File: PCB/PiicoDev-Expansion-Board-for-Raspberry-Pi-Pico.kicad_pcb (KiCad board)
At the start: 2 copper layers, 50.4 x 51.4 mm, 34 parts, among them J1 PiicoDev, J2 JST PH, J3 , J4 , Q1 MOSFET P-CH

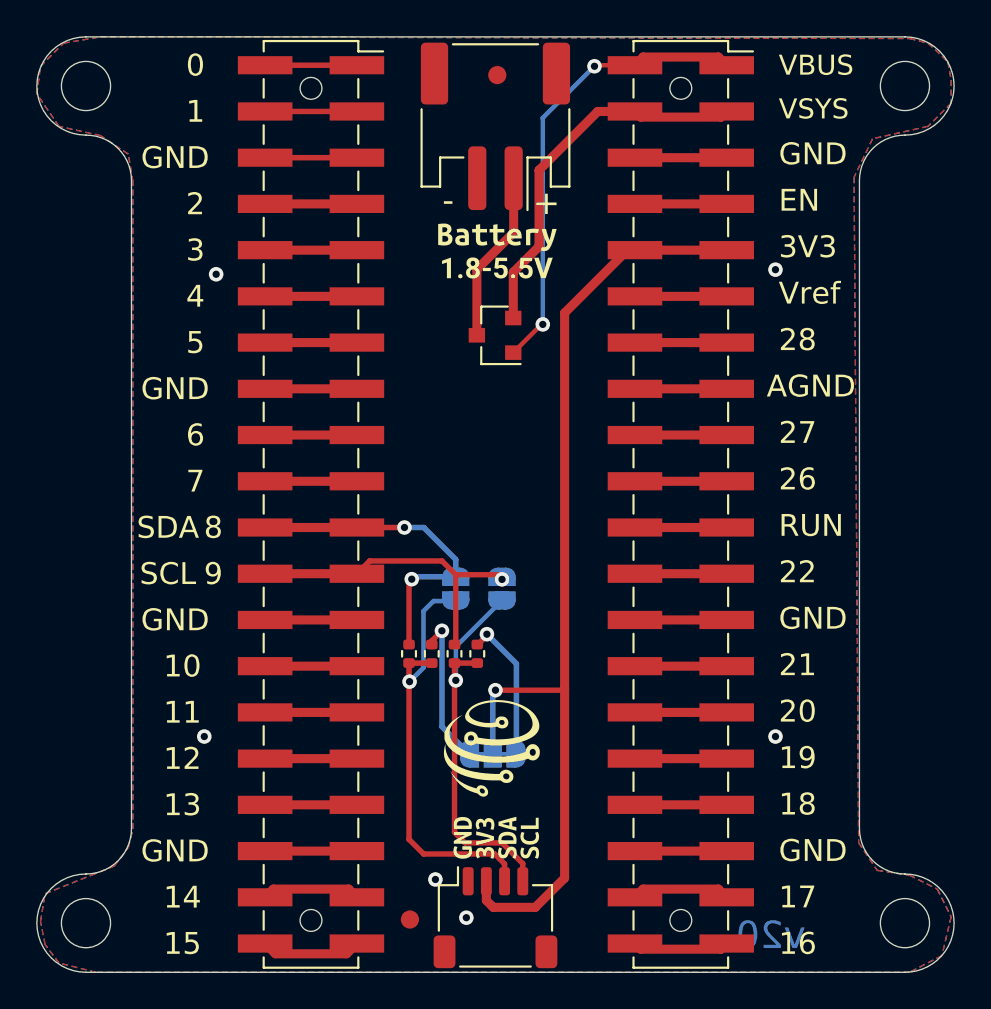
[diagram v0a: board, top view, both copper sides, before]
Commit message: Wide voltage expansion board
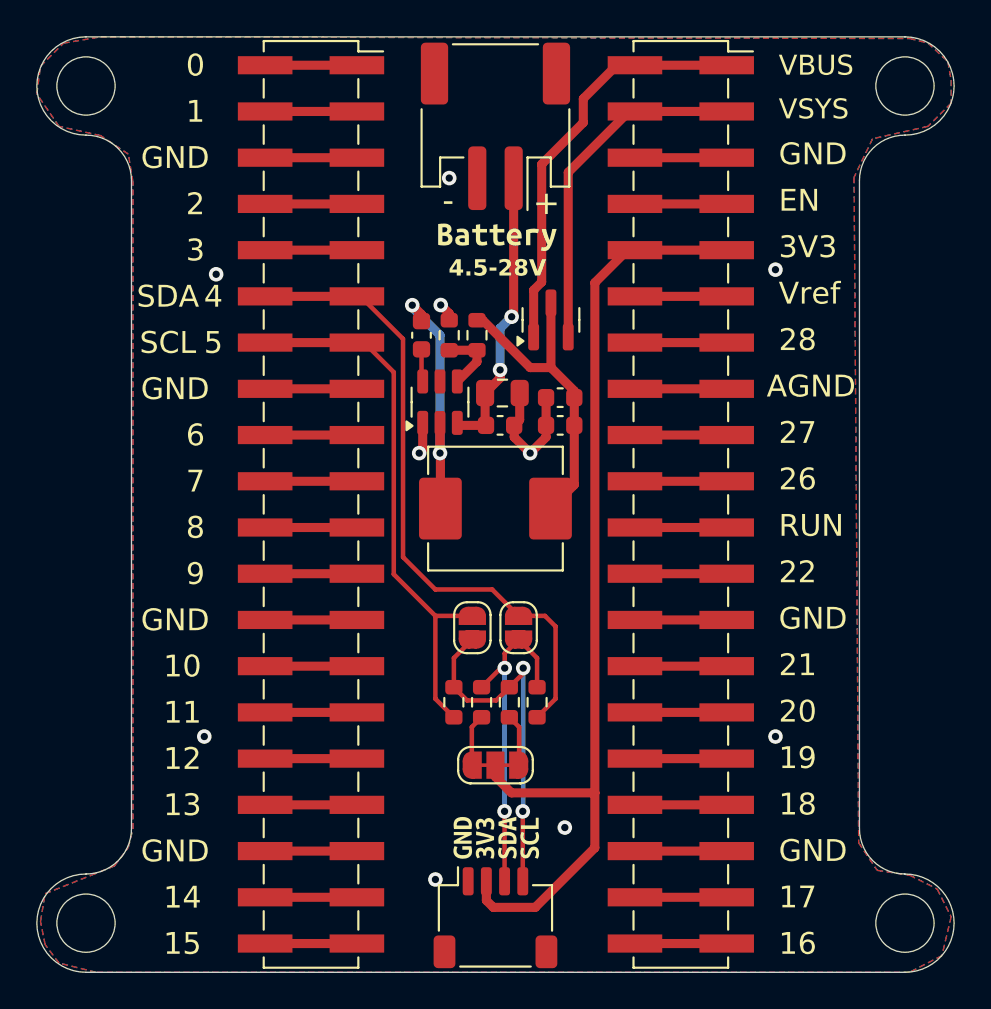
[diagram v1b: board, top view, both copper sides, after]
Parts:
- removed FID1, FID2: Fiducial, Fiducial:Fiducial_1mm_Mask2mm
- removed G1: LOGO_CoreElectronics_made-with-love, CoreElectronics_Artwork:CoreElectronics_logo_5mm
- removed G2: LOGO_PiicoDev, CoreElectronics_Artwork:piicodev_logo_14.2x3.4mm
- removed kibuzzard-629D9149: G***, kibuzzard-629D9149
- removed kibuzzard-629D9427: G***, kibuzzard-629D9427
- removed kibuzzard-629D9699: G***, kibuzzard-629D9699
- removed kibuzzard-62AAB365: G***, kibuzzard-62AAB365
- removed kibuzzard-62AAC6E5: G***, kibuzzard-62AAC6E5
- removed kibuzzard-62AAC6F3: G***, kibuzzard-62AAC6F3
- added C1: 10uF, Capacitor_SMD:C_0805_2012Metric, F.Cu at (141.2, 92.5)
- added C2: 0.1uF, Capacitor_SMD:C_0603_1608Metric, F.Cu at (141.1, 94.2)
- added C3: 0.1uF, Capacitor_SMD:C_0603_1608Metric, F.Cu at (136.8, 89.3)
- added C4: 22uF, Capacitor_SMD:C_0603_1608Metric, F.Cu at (144.4, 92.7)
- added C5: 22uF, Capacitor_SMD:C_0603_1608Metric, F.Cu at (144.4, 94.2)
- added L1: 10uF, Inductor_SMD:L_Abracon_ASPI-0630LR, F.Cu at (140.8, 98.8)
- added R1: 100k, Resistor_SMD:R_0603_1608Metric, F.Cu at (139.8, 89.3)
- added R2: 13.3k, Resistor_SMD:R_0603_1608Metric, F.Cu at (138.3, 89.3)
- added U1: TPS54302, Package_TO_SOT_SMD:SOT-23-6, F.Cu at (137.8, 93.0)
- H1, H2, H3, H4: footprint MountingHole:MountingHole_2.7mm_M2.5 -> MountingHole:MountingHole_3.2mm_M3
- JP1, JP2, JP3: moved to F.Cu
- R5, R6, R7, R8: footprint Resistor_SMD:R_0402_1005Metric -> Resistor_SMD:R_0603_1608Metric
- moved R7 7.52 mm to (143.1, 109.5), turned to 90 degrees
- moved JP1 4.06 mm to (142.1, 105.4)
- moved R5 3.82 mm to (140.1, 109.5), turned to 90 degrees
- moved R6 3.19 mm to (141.6, 109.5), turned to 90 degrees
- moved Q1 3.18 mm to (143.9, 88.5), turned to 90 degrees
- moved JP2 2.70 mm to (139.6, 105.4)
- moved R8 2.66 mm to (138.5, 109.5), turned to 90 degrees
- moved JP3 0.64 mm to (140.8, 112.9)
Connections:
- J3 pad 11: Net-(J3-Pad11) -> /I2C0_SDA
- J3 pad 12: Net-(J3-Pad11) -> /I2C0_SDA
- J3 pad 13: Net-(J3-Pad13) -> /I2C0_SCL
- J3 pad 14: Net-(J3-Pad13) -> /I2C0_SCL
- J3 pad 21: /I2C0_SDA -> Net-(#U2-GP8)
- J3 pad 22: /I2C0_SDA -> Net-(#U2-GP8)
- J3 pad 23: /I2C0_SCL -> Net-(#U2-GP9)
- J3 pad 24: /I2C0_SCL -> Net-(#U2-GP9)
- Q1 pad 3: VBAT -> +5V
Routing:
- net /I2C0_SDA: track 18.3 -> 35.9 mm, vias 2 -> 0
- net +5V: track 0.00 -> 17.5 mm
- net Net-(U1-SW): track 0.00 -> 14.6 mm, vias 0 -> 2
- net /I2C0_SCL: track 17.7 -> 30.1 mm, vias 1 -> 0
- net GND: track 36.9 -> 46.9 mm, vias 6 -> 10
- net Net-(J1-Pin_3): track 24.9 -> 18.4 mm, vias 1 -> 2
- net VBAT: track 9.47 -> 15.9 mm, vias 0 -> 2
- net Net-(JP3-B): track 8.37 -> 2.85 mm, vias 1 -> 0
- net Net-(JP3-A): track 8.06 -> 2.85 mm, vias 1 -> 0
- net Net-(J3-Pad13): track 5.04 -> 0.00 mm
- net Net-(J3-Pad11): track 5.04 -> 0.00 mm
- net Net-(#U2-GP9): track 0.00 -> 5.04 mm
- net Net-(#U2-GP8): track 0.00 -> 5.04 mm
- net Net-(U1-FB): track 0.00 -> 3.69 mm
- net VBUS: track 25.3 -> 22.9 mm, vias 2 -> 0
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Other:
- board text added: "4.5-28V"
- board text added: "Battery Packs: 4.5 - 28V"
- board text added: "Steel Bar Robotics CC BY-SA 4.0"
- board text added: "Suitable for"
- board text added: "Wide Voltage Version"
- board text removed: "v20"

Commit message: prototype production
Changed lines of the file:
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@@
 			)
 		)
-		(property "LCSC" "C2845363"
+		(property "LCSC" "C160404"
 			(at 0 0 0)
 			(unlocked yes)
@@
 		(sheetname "Root")
 		(sheetfile "PiicoDev-Expansion-Board-for-Raspberry-Pi-Pico.kicad_sch")
-		(attr exclude_from_pos_files)
+		(attr exclude_from_pos_files exclude_from_bom)
 		(fp_circle
 			(center 0 0)
@@
 		)
 		(fp_text user "${REFERENCE}"
-			(at 0 0 360)
+			(at 0 0 0)
 			(layer "F.Fab")
 			(hide yes)
@@
 		(sheetname "Root")
 		(sheetfile "PiicoDev-Expansion-Board-for-Raspberry-Pi-Pico.kicad_sch")
-		(attr exclude_from_pos_files)
+		(attr exclude_from_pos_files exclude_from_bom)
 		(fp_circle
 			(center 0 0)
@@
 		(sheetname "Root")
 		(sheetfile "PiicoDev-Expansion-Board-for-Raspberry-Pi-Pico.kicad_sch")
-		(attr exclude_from_pos_files)
+		(attr exclude_from_pos_files exclude_from_bom)
 		(fp_circle
 			(center 0 0)
@@
 		(sheetname "Root")
 		(sheetfile "PiicoDev-Expansion-Board-for-Raspberry-Pi-Pico.kicad_sch")
-		(attr exclude_from_pos_files)
+		(attr exclude_from_pos_files exclude_from_bom)
 		(fp_circle
 			(center 0 0)
@@
 		(sheetname "Root")
 		(sheetfile "PiicoDev-Expansion-Board-for-Raspberry-Pi-Pico.kicad_sch")
-		(attr exclude_from_pos_files)
+		(attr exclude_from_pos_files exclude_from_bom)
 		(fp_line
 			(start -0.7 1)
@@
 		)
 		(property "Value" "I2C"
-			(at 0 1.9 360)
+			(at 0 1.9 0)
 			(layer "F.Fab")
 			(effects
@@
 		)
 		(property "Footprint" "CoreElectronics_Components:SolderJumper-3_P1.3mm_Closed_RoundedPad1.0x1.5mm"
-			(at 0 0 360)
+			(at 0 0 0)
 			(layer "B.Fab")
 			(hide yes)
@@
 		)
 		(property "Datasheet" ""
-			(at 0 0 360)
+			(at 0 0 0)
 			(layer "B.Fab")
 			(hide yes)
@@
 		)
 		(property "Description" ""
-			(at 0 0 360)
+			(at 0 0 0)
 			(layer "B.Fab")
 			(hide yes)
@@
 		(sheetname "Root")
 		(sheetfile "PiicoDev-Expansion-Board-for-Raspberry-Pi-Pico.kicad_sch")
-		(attr exclude_from_pos_files)
+		(attr exclude_from_pos_files exclude_from_bom)
 		(net_tie_pad_groups "1, 2, 3")
 		(fp_line
@@
 		)
 		(property "Value" "0.1uF"
-			(at 0 1.43 360)
+			(at 0 1.43 0)
 			(layer "F.Fab")
 			(effects
@@
 		)
 		(fp_text user "${REFERENCE}"
-			(at 0 0 360)
+			(at 0 0 0)
 			(layer "F.Fab")
 			(effects
@@
 		)
 		(property "Value" "10uF"
-			(at 0 1.68 360)
+			(at 0 1.68 0)
 			(layer "F.Fab")
 			(effects
@@
 		)
 		(fp_text user "${REFERENCE}"
-			(at 0 0 360)
+			(at 0 0 0)
 			(layer "F.Fab")
 			(effects
@@
 		)
 		(property "Value" "22uF"
-			(at 0 1.43 360)
+			(at 0 1.43 0)
 			(layer "F.Fab")
 			(effects
@@
 		)
 		(fp_text user "${REFERENCE}"
-			(at 0 0 360)
+			(at 0 0 0)
 			(layer "F.Fab")
 			(effects
@@
 		)
 		(property "Value" "22uF"
-			(at 0 1.43 360)
+			(at 0 1.43 0)
 			(layer "F.Fab")
 			(effects
@@
 		)
 		(fp_text user "${REFERENCE}"
-			(at 0 0 360)
+			(at 0 0 0)
 			(layer "F.Fab")
 			(effects
@@
 		(sheetname "Root")
 		(sheetfile "PiicoDev-Expansion-Board-for-Raspberry-Pi-Pico.kicad_sch")
-		(attr exclude_from_pos_files)
+		(attr exclude_from_pos_files exclude_from_bom)
 		(fp_line
 			(start 0.7 -1)
@@
 		(start 136.771 90.071)
 		(end 136.771 91.77)
-		(width 0.25)
+		(width 0.5)
 		(layer "F.Cu")
 		(net 40)
